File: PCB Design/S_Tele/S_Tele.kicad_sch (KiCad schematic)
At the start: 33 parts, among them J1 Screw_Terminal_01x08, J2 Conn_01x01, J3 SMA, J4 SMA, J5 SMA, J6 SMA, J7 SMA, J8 SMA, U1 L7815, U2 L7805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

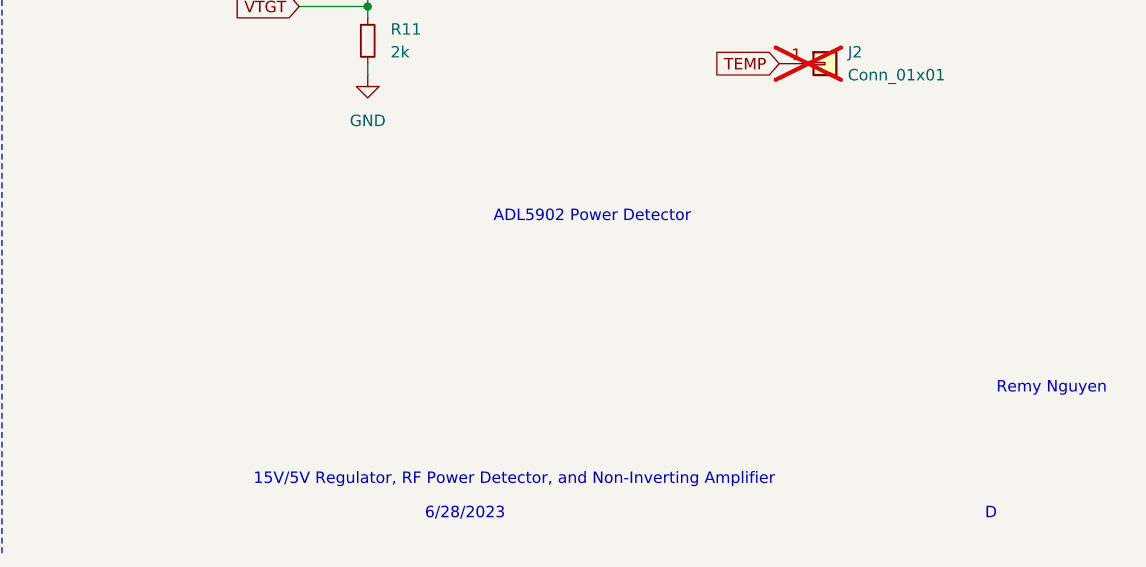
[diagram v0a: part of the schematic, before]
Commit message: Added output scaling circuit to report
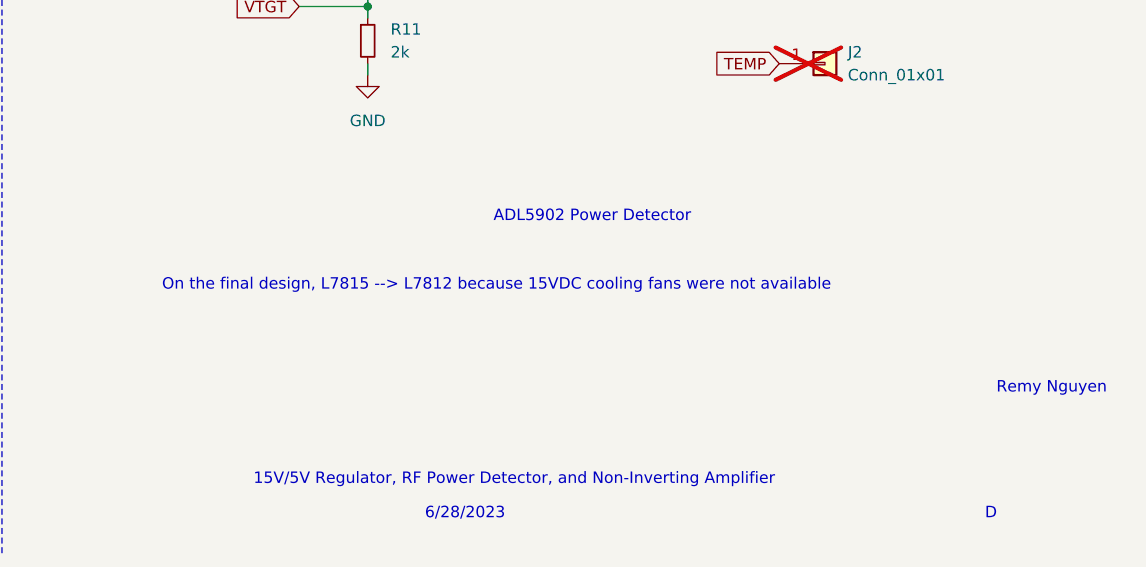
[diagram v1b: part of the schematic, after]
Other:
- note added: "On the final design, L7815 --> L7812 because 15VDC cooling fans were not available"
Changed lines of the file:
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@@
+    (effects (font (size 1.27 1.27)) (justify left bottom))
+  )
+  (text "On the final design, L7815 --> L7812 because 15VDC cooling fans were not available"
+    (at 177.8 168.91 0)
     (effects (font (size 1.27 1.27)) (justify left bottom))
   )
